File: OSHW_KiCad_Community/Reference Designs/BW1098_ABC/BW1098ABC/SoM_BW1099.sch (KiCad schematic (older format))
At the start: 29 parts

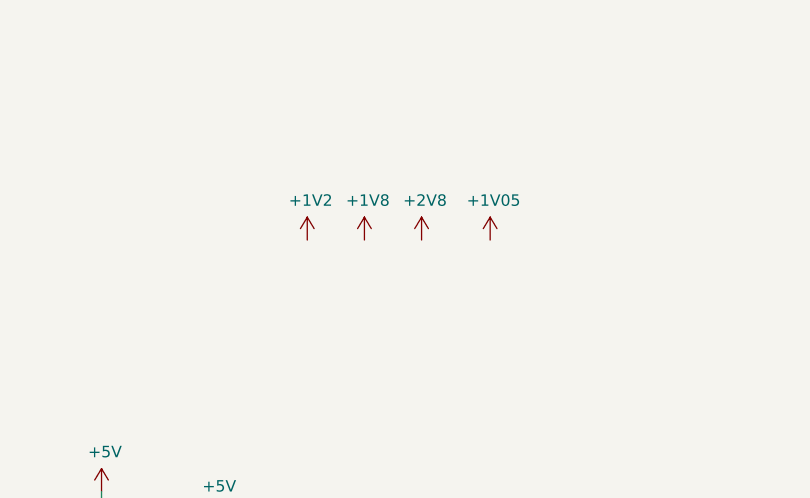
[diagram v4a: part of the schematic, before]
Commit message: added datasheets for everything but resistors caps and inductors
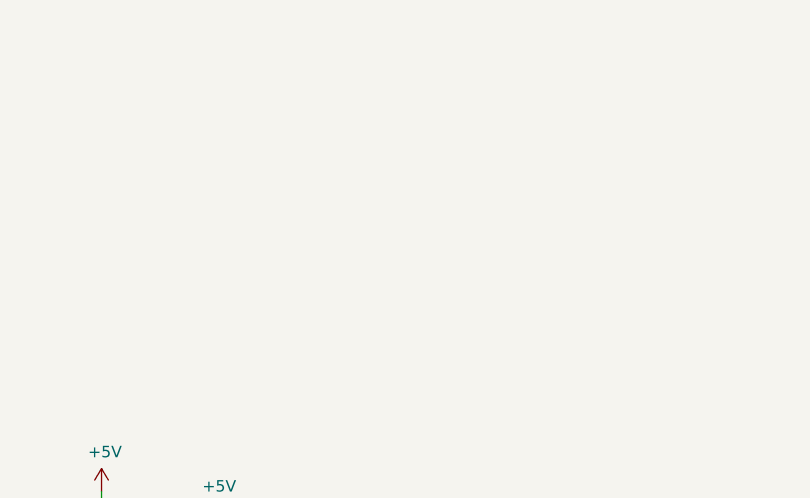
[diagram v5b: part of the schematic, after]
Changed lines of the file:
@@
 F 1 "DF40HC(3.0)-100DS-0.4V_BW1099_G2" H 8450 2983 60  0000 C CNN
 F 2 "fp_luxonis:HRS_DF40HC(3.0)-100DS-0.4V(58" H 7250 2800 60  0001 C CNN
-F 3 "" H 7250 2800 60  0000 C CNN
+F 3 "https://www.hirose.com/product/document?clcode=CL0684-4003-3-51&productname=DF40C-60DP-0.4V(51)&series=DF40&documenttype=Catalog&lang=en&documentid=D31649_en" H 7250 2800 60  0001 C CNN
 	1    7250 2800
 	1    0    0    -1
@@
 	1    0    0    -1
 $EndComp
-$Comp
-L power:+1V2 #PWR?
-U 1 1 60025A1E
-P 2250 1850
-F 0 "#PWR?" H 2250 1700 50  0001 C CNN
-F 1 "+1V2" H 2265 2023 50  0000 C CNN
-F 2 "" H 2250 1850 50  0001 C CNN
-F 3 "" H 2250 1850 50  0001 C CNN
-	1    2250 1850
-	1    0    0    -1
-$EndComp
-$Comp
-L power:+1V8 #PWR?
-U 1 1 60025A24
-P 2500 1850
-F 0 "#PWR?" H 2500 1700 50  0001 C CNN
-F 1 "+1V8" H 2515 2023 50  0000 C CNN
-F 2 "" H 2500 1850 50  0001 C CNN
-F 3 "" H 2500 1850 50  0001 C CNN
-	1    2500 1850
-	1    0    0    -1
-$EndComp
-$Comp
-L power:+2V8 #PWR?
-U 1 1 60025A2A
-P 2750 1850
-F 0 "#PWR?" H 2750 1700 50  0001 C CNN
-F 1 "+2V8" H 2765 2023 50  0000 C CNN
-F 2 "" H 2750 1850 50  0001 C CNN
-F 3 "" H 2750 1850 50  0001 C CNN
-	1    2750 1850
-	1    0    0    -1
-$EndComp
-$Comp
-L BW1098ABC-rescue:+1V05-depthAI_sch #PWR?
-U 1 1 60025A30
-P 3050 1850
-F 0 "#PWR?" H 3050 1700 50  0001 C CNN
-F 1 "+1V05" H 3065 2023 50  0000 C CNN
-F 2 "" H 3050 1850 50  0001 C CNN
-F 3 "" H 3050 1850 50  0001 C CNN
-	1    3050 1850
-	1    0    0    -1
-$EndComp

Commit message: added busses, fixed hierarchical labeling, just need to fix an erc thing with my buses then itll pass
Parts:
- removed D?: BAS16XV2T1G, Diode_SMD:D_SOD-523, symbol Diode:BAS16W
- removed R? (x2): 10KOHM-0603, Resistor_SMD:R_0603_1608Metric, symbol BW1098ABC-rescue:10KOHM-0603-1_10W-1%-SparkFun-Resistors
- removed U?: PMS150C-U06, symbol BW1098ABC-rescue:PMS150C-U06-depthAI_sch
- added MISC1: Layout_Guide_BW1099, symbol depthAI_sch:Layout_Guide_BW1099
- gave numbers to parts that had none: 25
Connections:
- net VDD_5V is gone; now on net +5V: J3.48 (5V), J3.50 (5V), J3.52 (5V), J3.54 (5V), TP4.1 (P)
- net +5V: now also J3.53 (5V)
- net I2C1_SCL: now also J3.33 (CAMA_I2C_SDA); no longer J3.35 (CAMA_I2C_SCL)
- net I2C1_SDA: now also J3.35 (CAMA_I2C_SCL); no longer J3.33 (CAMA_I2C_SDA)
- net MIPI_RX4_C_N renamed A1
- net MIPI_RX4_C_P renamed A2
- net MIPI_RX4_D0_N renamed A3
- net MIPI_RX4_D0_P renamed A4
- net MIPI_RX4_D1_N renamed A5
- net MIPI_RX4_D1_P renamed A6
- net MIPI_RX5_D2_N renamed A7
- net MIPI_RX5_D2_P renamed A8
- net MIPI_RX5_D3_N renamed A9
- net MIPI_RX5_D3_P renamed A10
- no-connect marks 0 -> 6
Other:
- note removed: "MIPI_CAM_A"
- note removed: "MIPI_CAM_B"
- note removed: "Slow ramp on PRST# \nfrom RC during POR"
- moved on the sheet: B1, H5, H6, H7, H8, J3, TP1, TP2, TP3, TP4, TP5

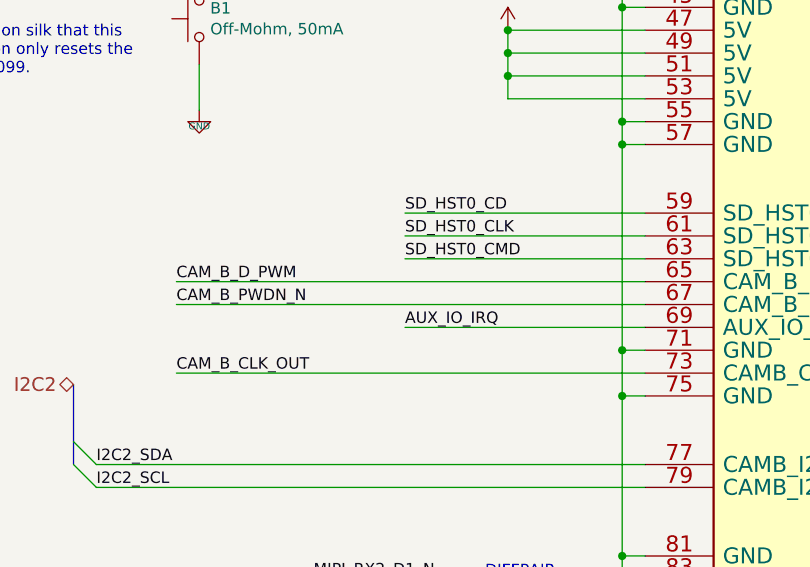
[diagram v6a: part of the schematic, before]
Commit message: made footprint for BW1099 layout guide. Just missing one small header and then need to complete the BBR43 which is pending some help from brandon
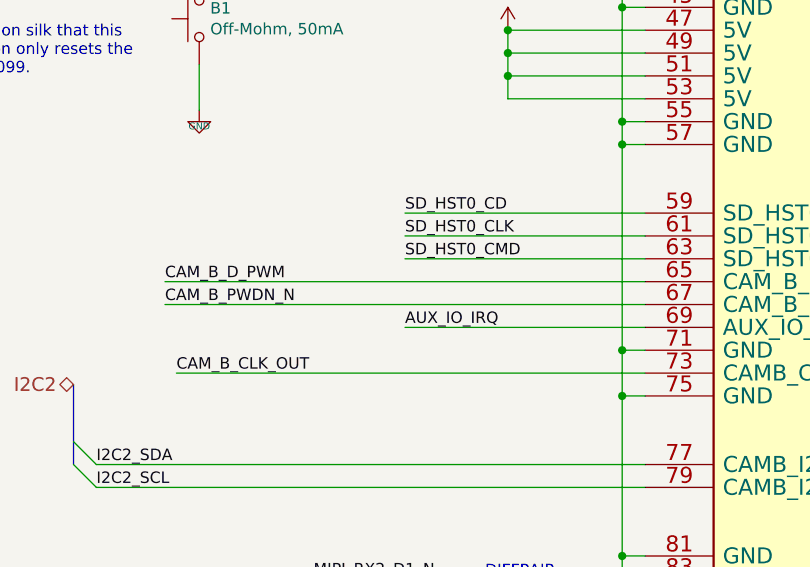
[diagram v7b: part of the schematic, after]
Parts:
- MISC1: footprint (none) -> fp_luxonis:BW1099_Layout_Guide
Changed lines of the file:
@@
 F 0 "MISC1" H 10628 2447 58  0000 L CNN
 F 1 "Layout_Guide_BW1099" H 10628 2344 58  0000 L CNN
-F 2 "" H 10050 2750 58  0001 C CNN
+F 2 "fp_luxonis:BW1099_Layout_Guide" H 10050 2750 58  0001 C CNN
 F 3 "" H 10050 2750 58  0001 C CNN
 F 4 "DNP" H 10628 2247 50  0000 L CNN "Population"
@@
 Entry Wire Line
 	12950 8950 13050 9050
-Text Label 7050 6950 0    50   ~ 0
+Text Label 7000 6950 0    50   ~ 0
 CAM_B_D_PWM
-Text Label 7050 7050 0    50   ~ 0
+Text Label 7000 7050 0    50   ~ 0
 CAM_B_PWDN_N
 Text Label 7050 7350 0    50   ~ 0
@@
 Wire Wire Line
 	7050 7350 9100 7350
-Wire Wire Line
-	9100 7050 7050 7050
-Wire Wire Line
-	7050 6950 9100 6950
 Text Label 8050 6650 0    50   ~ 0
 SD_HST0_CD
@@
 Wire Wire Line
 	1500 850  1900 850
+Wire Wire Line
+	7000 6950 9100 6950
+Wire Wire Line
+	7000 7050 9100 7050
 Wire Bus Line
 	5150 4250 5150 5350
